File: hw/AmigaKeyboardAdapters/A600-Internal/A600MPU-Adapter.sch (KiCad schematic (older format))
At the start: 9 parts, among them P1 CONN_02X03, P2 CONN_01X03, U1 6571R4_PLCC44_MPUKEY_REV

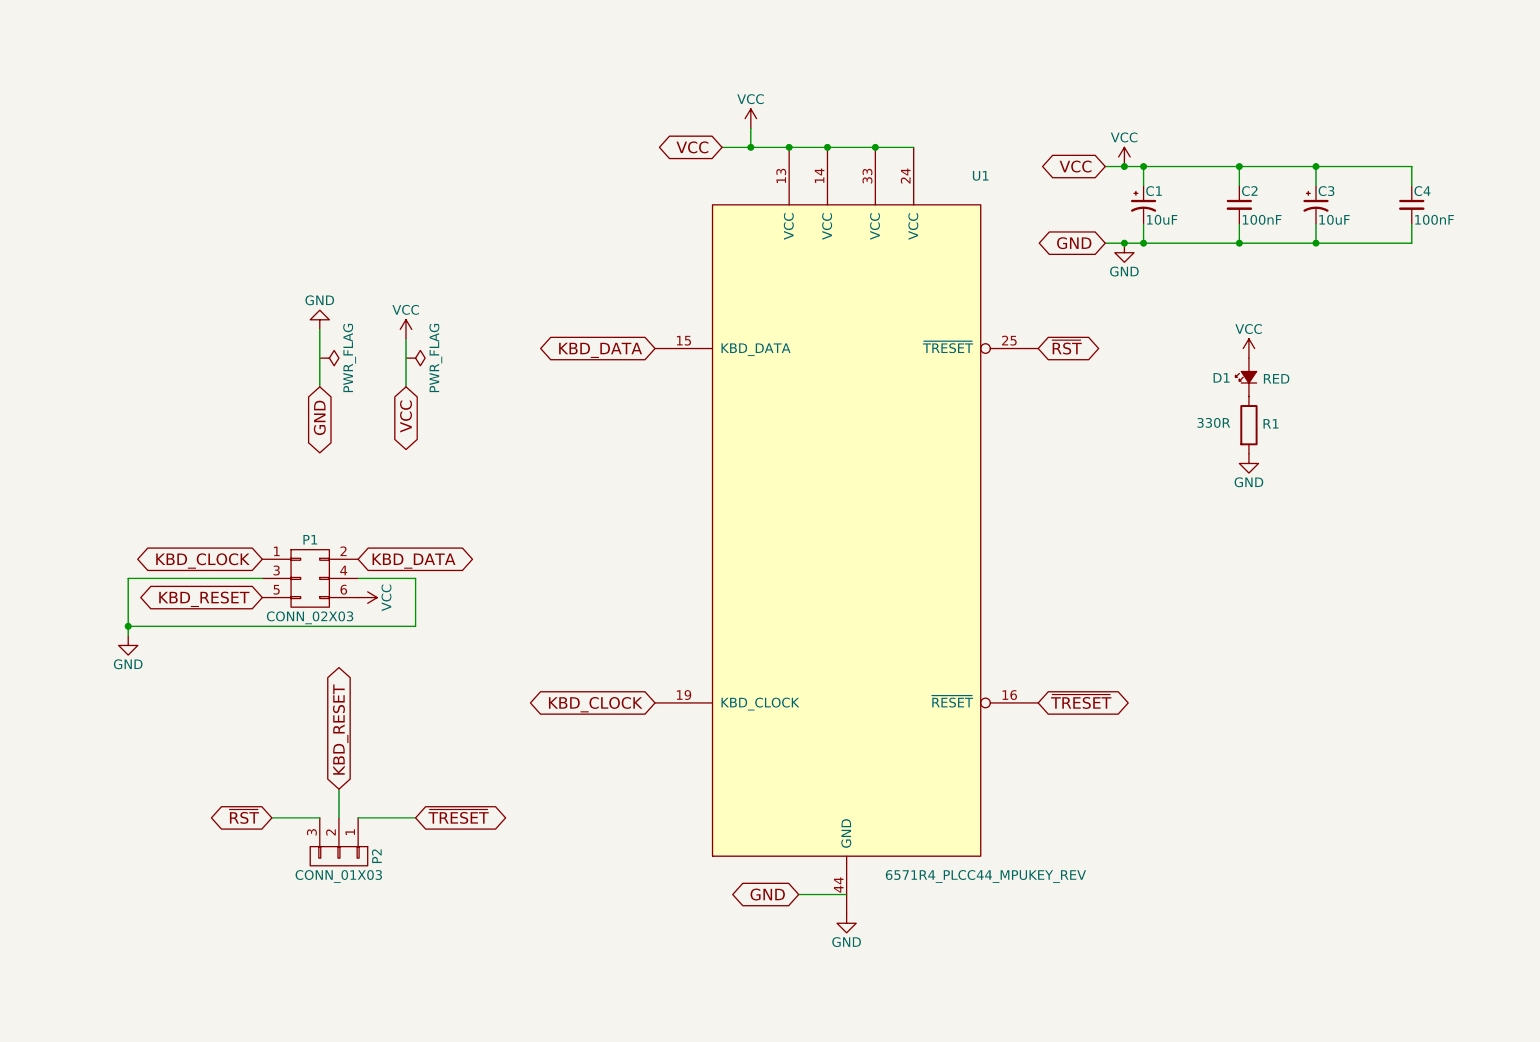
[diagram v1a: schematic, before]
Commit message: Updated PWR_FLAGs and other symbols
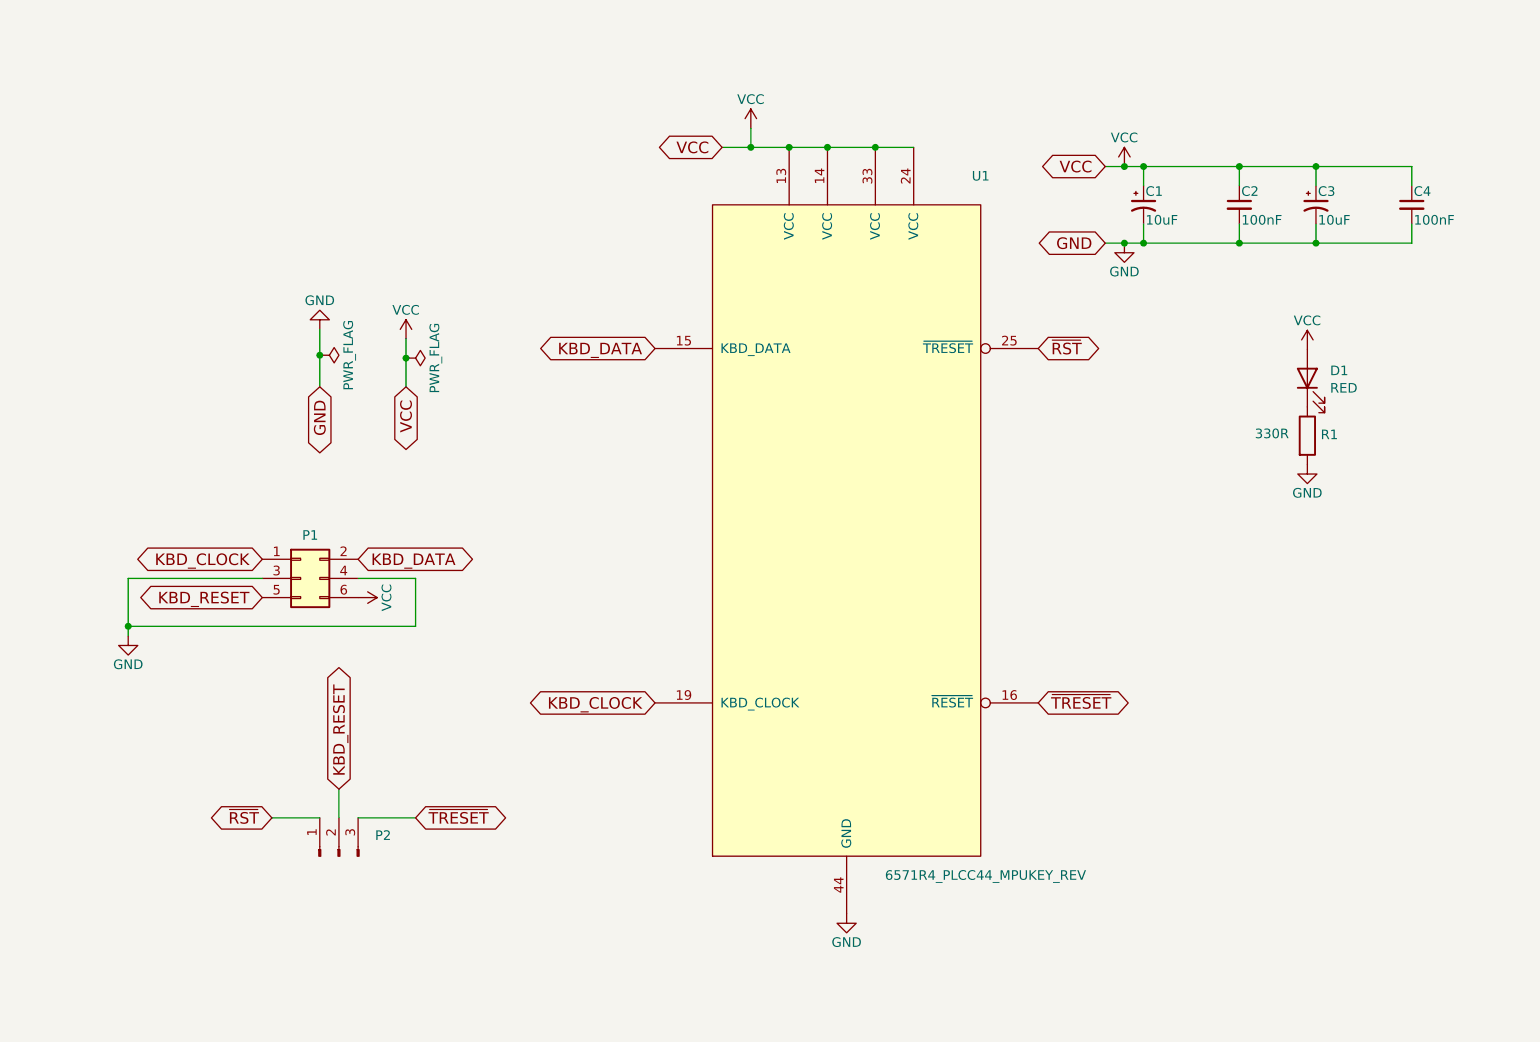
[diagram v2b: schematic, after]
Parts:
- removed D1: RED, LED_SMD:LED_1206_3216Metric_Pad1.42x1.75mm_HandSolder, symbol A600MPU-Adapter-rescue:Led_Small
- removed P1: CONN_02X03, Connector_IDC:IDC-Header_2x03_P2.54mm_Vertical, symbol A600MPU-Adapter-rescue:CONN_02X03
- removed P2: CONN_01X03, Connector_PinHeader_2.54mm:PinHeader_1x03_P2.54mm_Vertical, symbol A600MPU-Adapter-rescue:CONN_01X03
- added D1: RED, LED_SMD:LED_1206_3216Metric_Pad1.42x1.75mm_HandSolder, symbol Device:LED
- added P1: Conn_02x03_Odd_Even, Connector_IDC:IDC-Header_2x03_P2.54mm_Vertical, symbol Connector_Generic:Conn_02x03_Odd_Even
- added P2: Conn_01x03_Male, Connector_PinHeader_2.54mm:PinHeader_1x03_P2.54mm_Vertical, symbol Connector:Conn_01x03_Male
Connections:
- wire segments 36 -> 37
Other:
- moved on the sheet: R1
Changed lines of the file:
@@
 Text GLabel 4050 3050 3    60   BiDi ~ 0
 VCC
-Text GLabel 6100 5700 0    60   BiDi ~ 0
-GND
 Text GLabel 3800 3950 2    60   BiDi ~ 0
 KBD_DATA
@@
 Text GLabel 5350 4700 0    60   BiDi ~ 0
 KBD_CLOCK
-$Comp
-L A600MPU-Adapter-rescue:CONN_02X03 P1
-U 1 1 5BECAC1D
-P 3550 4050
-F 0 "P1" H 3550 4250 50  0000 C CNN
-F 1 "CONN_02X03" H 3550 3850 50  0000 C CNN
-F 2 "Connector_IDC:IDC-Header_2x03_P2.54mm_Vertical" H 3550 2850 50  0001 C CNN
-F 3 "" H 3550 2850 50  0000 C CNN
-	1    3550 4050
-	1    0    0    -1
-$EndComp
 Text GLabel 7350 4700 2    60   BiDi ~ 0
 ~TRESET
-$Comp
-L power:GND #PWR04
-U 1 1 5BECAD5B
-P 6350 5800
-F 0 "#PWR04" H 6350 5550 50  0001 C CNN
-F 1 "GND" H 6350 5650 50  0000 C CNN
-F 2 "" H 6350 5800 50  0001 C CNN
-F 3 "" H 6350 5800 50  0001 C CNN
-	1    6350 5800
-	1    0    0    -1
-$EndComp
-Wire Wire Line
-	6100 5700 6350 5700
-Wire Wire Line
-	6700 1800 6500 1800
 Wire Wire Line
 	5850 1700 5850 1800
 Connection ~ 5850 1800
-Connection ~ 6050 1800
-Connection ~ 6250 1800
-Connection ~ 6500 1800
-Wire Wire Line
-	4050 3050 4050 2800
+Wire Wire Line
+	4050 3050 4050 2900
 $Comp
 L power:VCC #PWR05
@@
 $EndComp
 Wire Wire Line
-	3600 2750 3600 3050
+	3600 2750 3600 2885
 Text GLabel 3600 3050 3    60   BiDi ~ 0
 GND
@@
 L power:PWR_FLAG #FLG07
 U 1 1 5BECAE1C
-P 3600 2900
-F 0 "#FLG07" H 3600 2975 50  0001 C CNN
-F 1 "PWR_FLAG" H 3600 3050 50  0000 C CNN
-F 2 "" H 3600 2900 50  0001 C CNN
-F 3 "" H 3600 2900 50  0001 C CNN
-	1    3600 2900
+P 3600 2885
+F 0 "#FLG07" H 3600 2960 50  0001 C CNN
+F 1 "PWR_FLAG" H 3600 3035 50  0000 C CNN
+F 2 "" H 3600 2885 50  0001 C CNN
+F 3 "" H 3600 2885 50  0001 C CNN
+	1    3600 2885
 	0    1    1    0
 $EndComp
@@
 	4100 4300 2600 4300
 Connection ~ 2600 4300
-$Comp
-L AmigaComponents:6571R4_PLCC44_MPUKEY_REV U1
-U 1 1 5BECAC84
-P 6350 3800
-F 0 "U1" H 7050 5650 50  0000 C CNN
-F 1 "6571R4_PLCC44_MPUKEY_REV" H 6550 2000 50  0000 L CNN
-F 2 "RetroBitLab:PLCC-44_THT-Socket_3D" H 6350 3800 60  0001 C CNN
-F 3 "" H 6350 3800 60  0000 C CNN
-	1    6350 3800
-	1    0    0    -1
-$EndComp
-$Comp
-L A600MPU-Adapter-rescue:CONN_01X03 P2
-U 1 1 5BECAF7D
-P 3700 5500
-F 0 "P2" H 3700 5700 50  0000 C CNN
-F 1 "CONN_01X03" V 3800 5500 50  0000 C CNN
-F 2 "Connector_PinHeader_2.54mm:PinHeader_1x03_P2.54mm_Vertical" H 3700 5500 50  0001 C CNN
-F 3 "" H 3700 5500 50  0000 C CNN
-	1    3700 5500
-	0    1    1    0
-$EndComp
 Wire Wire Line
 	3800 5300 4100 5300
@@
 Connection ~ 7800 1900
 $Comp
-L A600MPU-Adapter-rescue:Led_Small D1
-U 1 1 5BECB5FD
-P 8450 3000
-F 0 "D1" V 8445 3095 50  0000 L CNN
-F 1 "RED" V 8440 2785 50  0000 L CNN
-F 2 "LED_SMD:LED_1206_3216Metric_Pad1.42x1.75mm_HandSolder" V 8450 3000 50  0001 C CNN
-F 3 "https://datasheet.lcsc.com/lcsc/1811151241_Everlight-Elec-15-21-R6C-FQ1R1B-2T_C93133.pdf" V 8450 3000 50  0001 C CNN
-F 4 "C93133" V 8450 3000 50  0001 C CNN "LCSC"
-	1    8450 3000
-	0    -1   -1   0
-$EndComp
-$Comp
 L Device:R R1
 U 1 1 5BECB680
-P 8450 3250
-F 0 "R1" H 8565 3255 50  0000 C CNN
-F 1 "330R" H 8265 3260 50  0000 C CNN
-F 2 "Resistor_SMD:R_1206_3216Metric_Pad1.30x1.75mm_HandSolder" V 8380 3250 50  0001 C CNN
-F 3 "https://datasheet.lcsc.com/lcsc/1811141443_Ever-Ohms-Tech-CR1206F330RP05Z_C245520.pdf" H 8450 3250 50  0001 C CNN
-F 4 "C245520" H 8450 3250 50  0001 C CNN "LCSC"
-	1    8450 3250
-	1    0    0    -1
-$EndComp
-$Comp
-L power:VCC #PWR011
-U 1 1 5BECB6C0
-P 8450 2900
-F 0 "#PWR011" H 8450 2750 50  0001 C CNN
-F 1 "VCC" H 8450 3050 50  0000 C CNN
-F 2 "" H 8450 2900 50  0001 C CNN
-F 3 "" H 8450 2900 50  0001 C CNN
-	1    8450 2900
+P 8755 3305
+F 0 "R1" H 8870 3310 50  0000 C CNN
+F 1 "330R" H 8570 3315 50  0000 C CNN
+F 2 "Resistor_SMD:R_1206_3216Metric_Pad1.30x1.75mm_HandSolder" V 8685 3305 50  0001 C CNN
+F 3 "https://datasheet.lcsc.com/lcsc/1811141443_Ever-Ohms-Tech-CR1206F330RP05Z_C245520.pdf" H 8755 3305 50  0001 C CNN
+F 4 "C245520" H 8755 3305 50  0001 C CNN "LCSC"
+	1    8755 3305
 	1    0    0    -1
 $EndComp
@@
 L power:GND #PWR012
 U 1 1 5BECB6E6
-P 8450 3400
-F 0 "#PWR012" H 8450 3150 50  0001 C CNN
-F 1 "GND" H 8450 3250 50  0000 C CNN
-F 2 "" H 8450 3400 50  0001 C CNN
-F 3 "" H 8450 3400 50  0001 C CNN
-	1    8450 3400
+P 8755 3455
+F 0 "#PWR012" H 8755 3205 50  0001 C CNN
+F 1 "GND" H 8755 3305 50  0000 C CNN
+F 2 "" H 8755 3455 50  0001 C CNN
+F 3 "" H 8755 3455 50  0001 C CNN
+	1    8755 3455
 	1    0    0    -1
 $EndComp
 Wire Wire Line
 	5850 1800 5700 1800
-Wire Wire Line
-	6050 1800 5850 1800
-Wire Wire Line
-	6250 1800 6050 1800
-Wire Wire Line
-	6500 1800 6250 1800
 Wire Wire Line
 	2600 4300 2600 4350
@@
 	1    0    0    -1
 $EndComp
+Connection ~ 3600 2885
+Wire Wire Line
+	3600 2885 3600 3050
+Connection ~ 4050 2900
+Wire Wire Line
+	4050 2900 4050 2800
+$Comp
+L Device:LED D1
+U 1 1 63861A09
+P 8755 3005
+F 0 "D1" V 8794 2887 50  0000 R CNN
+F 1 "RED" V 8703 2887 50  0000 R CNN
+F 2 "LED_SMD:LED_1206_3216Metric_Pad1.42x1.75mm_HandSolder" H 8755 3005 50  0001 C CNN
+F 3 "https://datasheet.lcsc.com/lcsc/1811151241_Everlight-Elec-15-21-R6C-FQ1R1B-2T_C93133.pdf" H 8755 3005 50  0001 C CNN
+F 4 "C93133" V 8755 3005 50  0001 C CNN "LCSC"
+	1    8755 3005
+	0    -1   -1   0
+$EndComp
+$Comp
+L power:VCC #PWR011
+U 1 1 5BECB6C0
+P 8755 2855
+F 0 "#PWR011" H 8755 2705 50  0001 C CNN
+F 1 "VCC" H 8755 3005 50  0000 C CNN
+F 2 "" H 8755 2855 50  0001 C CNN
+F 3 "" H 8755 2855 50  0001 C CNN
+	1    8755 2855
+	1    0    0    -1
+$EndComp
+$Comp
+L Connector_Generic:Conn_02x03_Odd_Even P1
+U 1 1 63869AA4
+P 3500 4050
+F 0 "P1" H 3550 4275 50  0000 C CNN
+F 1 "Conn_02x03_Odd_Even" H 3550 4276 50  0001 C CNN
+F 2 "Connector_IDC:IDC-Header_2x03_P2.54mm_Vertical" H 3500 4050 50  0001 C CNN
+F 3 "~" H 3500 4050 50  0001 C CNN
+	1    3500 4050
+	1    0    0    -1
+$EndComp
+$Comp
+L Connector:Conn_01x03_Male P2
+U 1 1 6386C64E
+P 3700 5500
+F 0 "P2" V 3808 5312 50  0000 R CNN
+F 1 "Conn_01x03_Male" V 3763 5312 50  0001 R CNN
+F 2 "Connector_PinHeader_2.54mm:PinHeader_1x03_P2.54mm_Vertical" H 3700 5500 50  0001 C CNN
+F 3 "~" H 3700 5500 50  0001 C CNN
+	1    3700 5500
+	0    -1   -1   0
+$EndComp
+$Comp
+L AmigaComponents:6571R4_PLCC44_MPUKEY_REV U1
+U 1 1 5BECAC84
+P 6350 3800
+F 0 "U1" H 7050 5650 50  0000 C CNN
+F 1 "6571R4_PLCC44_MPUKEY_REV" H 6550 2000 50  0000 L CNN
+F 2 "RetroBitLab:PLCC-44_THT-Socket_3D" H 6350 3800 60  0001 C CNN
+F 3 "" H 6350 3800 60  0000 C CNN
+	1    6350 3800
+	1    0    0    -1
+$EndComp
+Wire Wire Line
+	5850 1800 6050 1800
+Wire Wire Line
+	6500 1800 6700 1800
+Wire Wire Line
+	6500 1800 6250 1800
+Connection ~ 6500 1800
+Wire Wire Line
+	6250 1800 6050 1800
+Connection ~ 6250 1800
+Connection ~ 6050 1800
+$Comp
+L power:GND #PWR?
+U 1 1 6388659D
+P 6350 5800
+F 0 "#PWR?" H 6350 5550 50  0001 C CNN
+F 1 "GND" H 6350 5650 50  0000 C CNN
+F 2 "" H 6350 5800 50  0001 C CNN
+F 3 "" H 6350 5800 50  0001 C CNN
+	1    6350 5800
+	1    0    0    -1
+$EndComp

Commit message: RetroBitLab library
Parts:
- U1: symbol AmigaComponents:6571R4_PLCC44_MPUKEY_REV -> RetroBitLab:6571R4_PLCC44_MPUKEY_REV
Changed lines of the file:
@@
 $EndComp
 $Comp
-L AmigaComponents:6571R4_PLCC44_MPUKEY_REV U1
+L RetroBitLab:6571R4_PLCC44_MPUKEY_REV U1
 U 1 1 5BECAC84
 P 6350 3800
